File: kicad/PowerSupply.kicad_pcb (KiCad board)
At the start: 2 copper layers, 93 x 116 mm, 115 parts, among them J1 USB_A, J2 Display, J3 USART, J4 Terminal, Q1 MMBT3904, Q2 MMBT3904, Q3 MMBT3904, Q4 MMBT3904, SW1 ENC0 (Voltage), SW2 ENC1 (Current)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

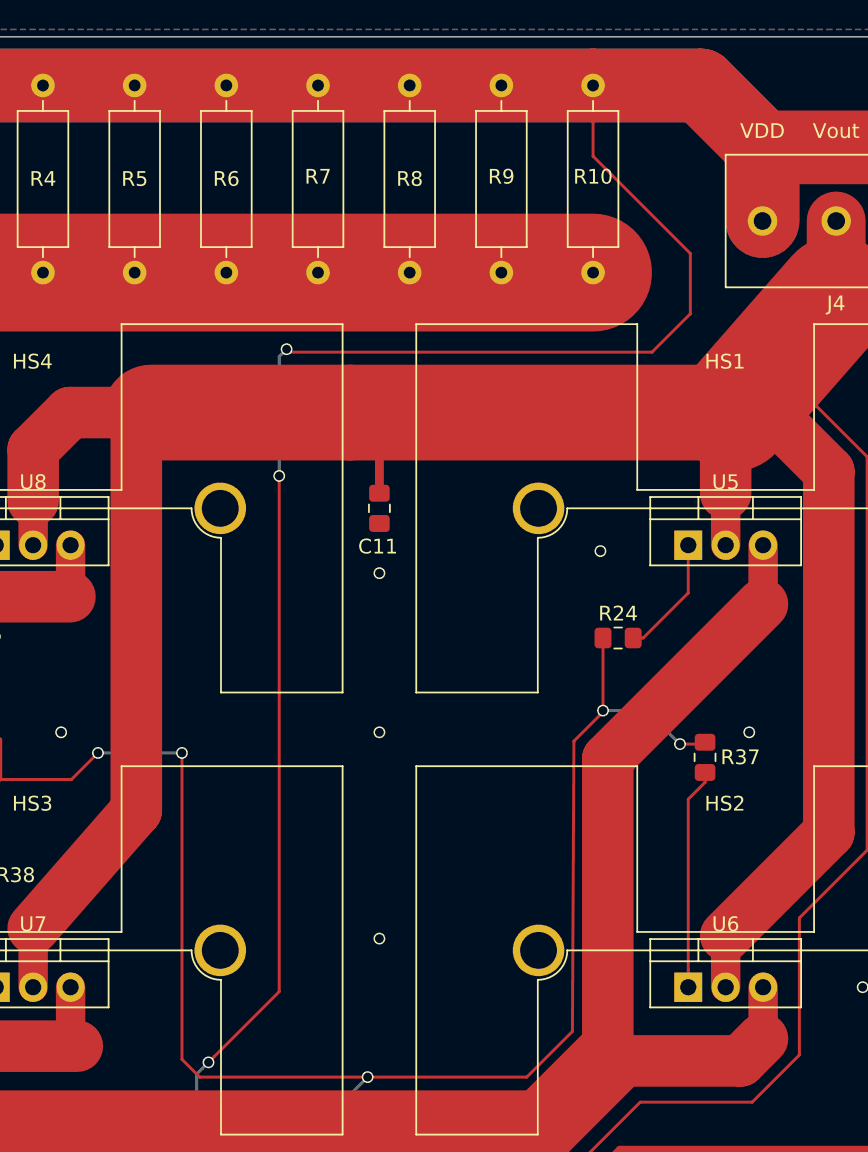
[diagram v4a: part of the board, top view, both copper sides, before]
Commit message: Moved via out of the heatsink area
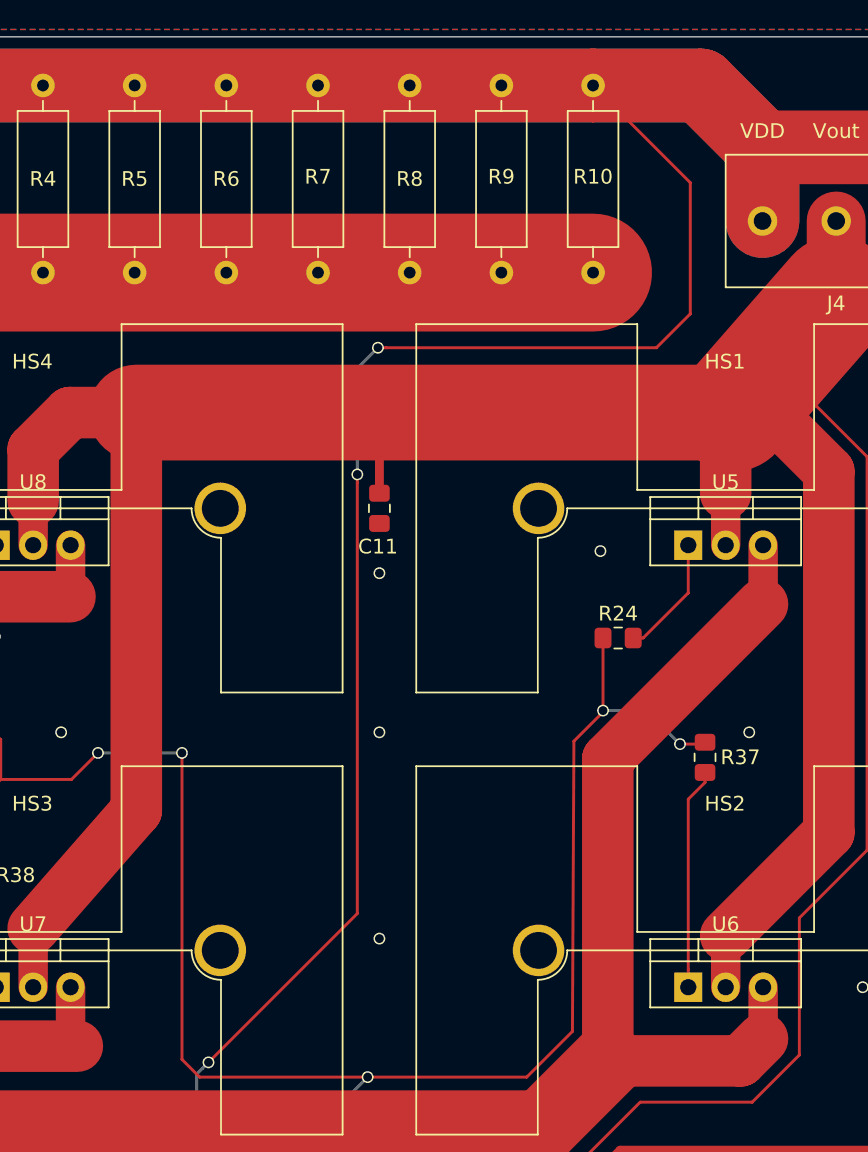
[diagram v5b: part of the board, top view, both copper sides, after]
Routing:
- net VDD: track 450.4 -> 446.6 mm
- net /Vout: track 256.7 -> 255.7 mm
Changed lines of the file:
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@@
     (thickness 1.6)
     (drawings 24)
-    (tracks 898)
+    (tracks 896)
     (zones 0)
     (modules 115)
@@
   (gr_line (start 0 0) (end 93 0) (layer Edge.Cuts) (width 0.05))
   (gr_line (start 0 0) (end 0 116) (layer Edge.Cuts) (width 0.05))
-  (segment (start 15.825 86) (end 15.825 85.025) (width 0.2) (layer F.Cu) (net 40))
-  (segment (start 13.775 84.675) (end 13.775 83.6) (width 0.2) (layer F.Cu) (net 40))
-  (segment (start 13.9 84.8) (end 13.775 84.675) (width 0.2) (layer F.Cu) (net 40))
-  (segment (start 15.825 85.025) (end 15.6 84.8) (width 0.2) (layer F.Cu) (net 40))
-  (segment (start 15.6 84.8) (end 13.9 84.8) (width 0.2) (layer F.Cu) (net 40))
   (via (at 5.2 91.7) (size 0.8) (drill 0.6) (layers F.Cu B.Cu) (net 1))
   (segment (start 8.25 88.25) (end 8.25 77.75) (width 0.2) (layer F.Cu) (net 1))
@@
   (segment (start 22.2 85) (end 20.025 85) (width 0.2) (layer F.Cu) (net 2))
   (segment (start 22.80001 84.39999) (end 22.2 85) (width 0.2) (layer F.Cu) (net 2))
-  (segment (start 62 3.3) (end 62 8.1) (width 0.2) (layer F.Cu) (net 2))
-  (segment (start 62 8.1) (end 68.6 14.7) (width 0.2) (layer F.Cu) (net 2))
-  (segment (start 68.6 14.7) (end 68.6 18.8) (width 0.2) (layer F.Cu) (net 2))
-  (segment (start 68.6 18.8) (end 66 21.4) (width 0.2) (layer F.Cu) (net 2))
-  (via (at 41.2 21.2) (size 0.8) (drill 0.6) (layers F.Cu B.Cu) (net 2))
-  (segment (start 66 21.4) (end 41.4 21.4) (width 0.2) (layer F.Cu) (net 2))
-  (segment (start 41.4 21.4) (end 41.2 21.2) (width 0.2) (layer F.Cu) (net 2))
-  (via (at 40.7 29.8) (size 0.8) (drill 0.6) (layers F.Cu B.Cu) (net 2))
-  (segment (start 41.2 21.2) (end 40.7 21.7) (width 0.2) (layer B.Cu) (net 2))
-  (segment (start 40.7 21.7) (end 40.7 29.8) (width 0.2) (layer B.Cu) (net 2))
   (segment (start 56.90001 84.39999) (end 52.65001 84.39999) (width 0.2) (layer F.Cu) (net 2))
   (segment (start 58.175 83.8) (end 57.5 83.8) (width 0.2) (layer F.Cu) (net 2))
@@
   (segment (start 35.100002 70.399998) (end 35.500001 69.999999) (width 0.2) (layer B.Cu) (net 2))
   (segment (start 35.100002 77.4) (end 35.100002 70.399998) (width 0.2) (layer B.Cu) (net 2))
-  (segment (start 36.299999 69.200001) (end 35.9 69.6) (width 0.2) (layer F.Cu) (net 2))
-  (segment (start 40.7 64.8) (end 36.299999 69.200001) (width 0.2) (layer F.Cu) (net 2))
-  (segment (start 40.7 29.8) (end 40.7 64.8) (width 0.2) (layer F.Cu) (net 2))
   (segment (start 35.500001 69.999999) (end 35.9 69.6) (width 0.2) (layer B.Cu) (net 2))
   (via (at 35.9 69.6) (size 0.8) (drill 0.6) (layers F.Cu B.Cu) (net 2))
   (segment (start 84.46 79.725) (end 84.46 73.54) (width 2) (layer F.Cu) (net 2))
+  (via (at 47.4 21.1) (size 0.8) (drill 0.6) (layers F.Cu B.Cu) (net 2))
+  (segment (start 62 3.3) (end 68.6 9.9) (width 0.2) (layer F.Cu) (net 2))
+  (segment (start 66.3 21.1) (end 47.965685 21.1) (width 0.2) (layer F.Cu) (net 2))
+  (segment (start 47.965685 21.1) (end 47.4 21.1) (width 0.2) (layer F.Cu) (net 2))
+  (segment (start 68.6 18.8) (end 66.3 21.1) (width 0.2) (layer F.Cu) (net 2))
+  (segment (start 68.6 9.9) (end 68.6 18.8) (width 0.2) (layer F.Cu) (net 2))
+  (via (at 46 29.699996) (size 0.8) (drill 0.6) (layers F.Cu B.Cu) (net 2))
+  (segment (start 46 22.5) (end 46 29.134311) (width 0.2) (layer B.Cu) (net 2))
+  (segment (start 46 29.134311) (end 46 29.699996) (width 0.2) (layer B.Cu) (net 2))
+  (segment (start 47.4 21.1) (end 46 22.5) (width 0.2) (layer B.Cu) (net 2))
+  (segment (start 46 30.265681) (end 46 29.699996) (width 0.2) (layer F.Cu) (net 2))
+  (segment (start 35.9 69.6) (end 46 59.5) (width 0.2) (layer F.Cu) (net 2))
+  (segment (start 46 59.5) (end 46 30.265681) (width 0.2) (layer F.Cu) (net 2))
   (segment (start 87 79.725) (end 87 88.875) (width 1) (layer F.Cu) (net 3))
   (segment (start 79.5 87.025) (end 85.15 87.025) (width 1) (layer F.Cu) (net 3))
@@
   (segment (start 78 54) (end 71 61) (width 3.5) (layer F.Cu) (net 8))
   (segment (start 71 61) (end 71 64.5) (width 2) (layer F.Cu) (net 8))
-  (segment (start 30 25.5) (end 32 25.5) (width 2) (layer F.Cu) (net 8))
   (segment (start 24 34.5) (end 24 31.5) (width 2) (layer F.Cu) (net 8))
   (segment (start 31 25.5) (end 31 52.5) (width 3.5) (layer F.Cu) (net 8))
@@
   (segment (start 47.5 27.5) (end 45.5 25.5) (width 0.6) (layer F.Cu) (net 8))
   (segment (start 47.5 30.975) (end 47.5 27.5) (width 0.6) (layer F.Cu) (net 8))
-  (segment (start 71.400002 25.5) (end 45.5 25.5) (width 6.5) (layer F.Cu) (net 8))
-  (segment (start 45.5 25.5) (end 32 25.5) (width 6.5) (layer F.Cu) (net 8))
   (segment (start 78.5 17.5) (end 71.5 25.5) (width 8) (layer F.Cu) (net 8))
+  (segment (start 71.400002 25.5) (end 31 25.5) (width 6.5) (layer F.Cu) (net 8))
   (segment (start 44.925 80.1) (end 49.2 80.1) (width 0.2) (layer F.Cu) (net 9))
   (segment (start 49.2 80.1) (end 49.875 79.425) (width 0.2) (layer F.Cu) (net 9))
@@
   (segment (start 15.835 81.19) (end 15.825 81.2) (width 0.2) (layer F.Cu) (net 39))
   (segment (start 20.025 81.19) (end 15.835 81.19) (width 0.2) (layer F.Cu) (net 39))
+  (segment (start 15.825 86) (end 15.825 85.025) (width 0.2) (layer F.Cu) (net 40))
+  (segment (start 13.775 84.675) (end 13.775 83.6) (width 0.2) (layer F.Cu) (net 40))
+  (segment (start 13.9 84.8) (end 13.775 84.675) (width 0.2) (layer F.Cu) (net 40))
+  (segment (start 15.825 85.025) (end 15.6 84.8) (width 0.2) (layer F.Cu) (net 40))
+  (segment (start 15.6 84.8) (end 13.9 84.8) (width 0.2) (layer F.Cu) (net 40))
   (segment (start 15.825 85.65) (end 15.825 85.9) (width 0.2) (layer F.Cu) (net 40))
   (segment (start 16.7 85.9) (end 15.825 85.9) (width 0.2) (layer F.Cu) (net 40))

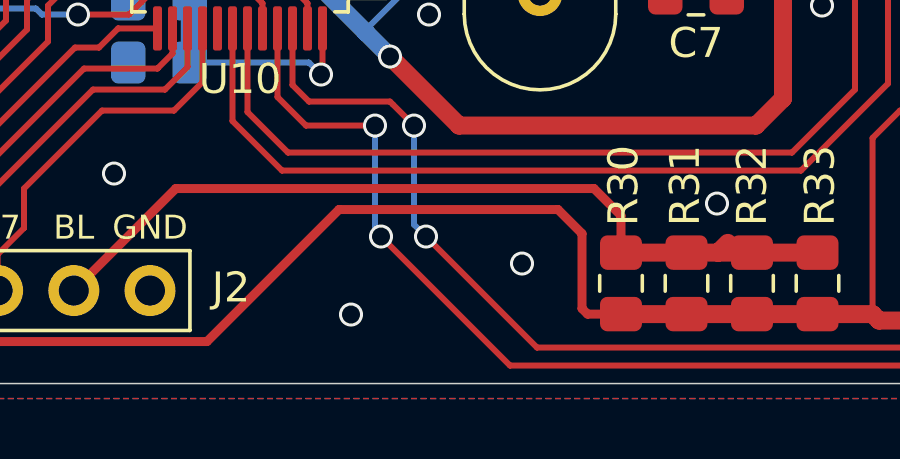
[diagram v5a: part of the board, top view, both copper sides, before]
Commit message: Added REV2 on silk
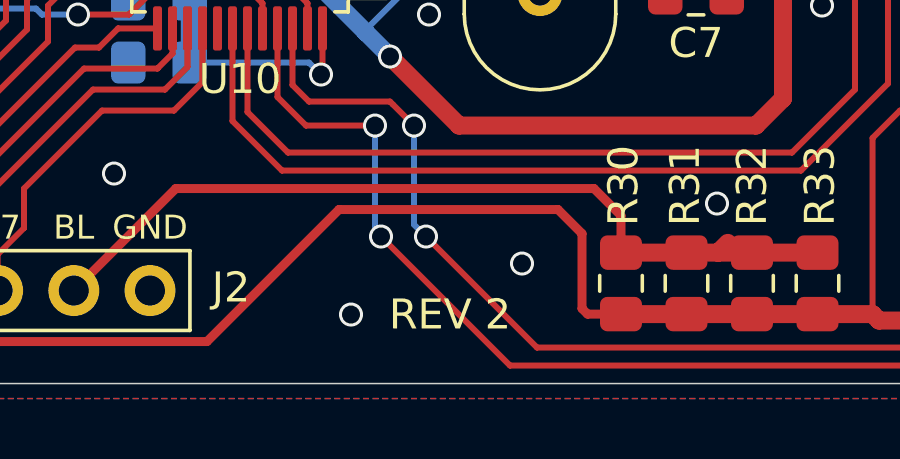
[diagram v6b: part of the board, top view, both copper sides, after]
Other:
- board text added: "REV 2"
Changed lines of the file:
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@@
   (general
     (thickness 1.6)
-    (drawings 24)
+    (drawings 25)
     (tracks 896)
     (zones 0)
@@
     )
   )
+  (gr_text "REV 2" (at 37 113.7) (layer F.SilkS)
+    (effects (font (size 1 1) (thickness 0.15)))
+  )
   (gr_text GND (at 27 110.8) (layer F.SilkS)
